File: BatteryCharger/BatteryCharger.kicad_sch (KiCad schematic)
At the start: 6 parts, among them Q1 SiR638DP, Q2 SiR638DP, Q3 SiR500DP, Q4 BSC059N04LS6, Q5 SQJ868EP, U1 BQ24735

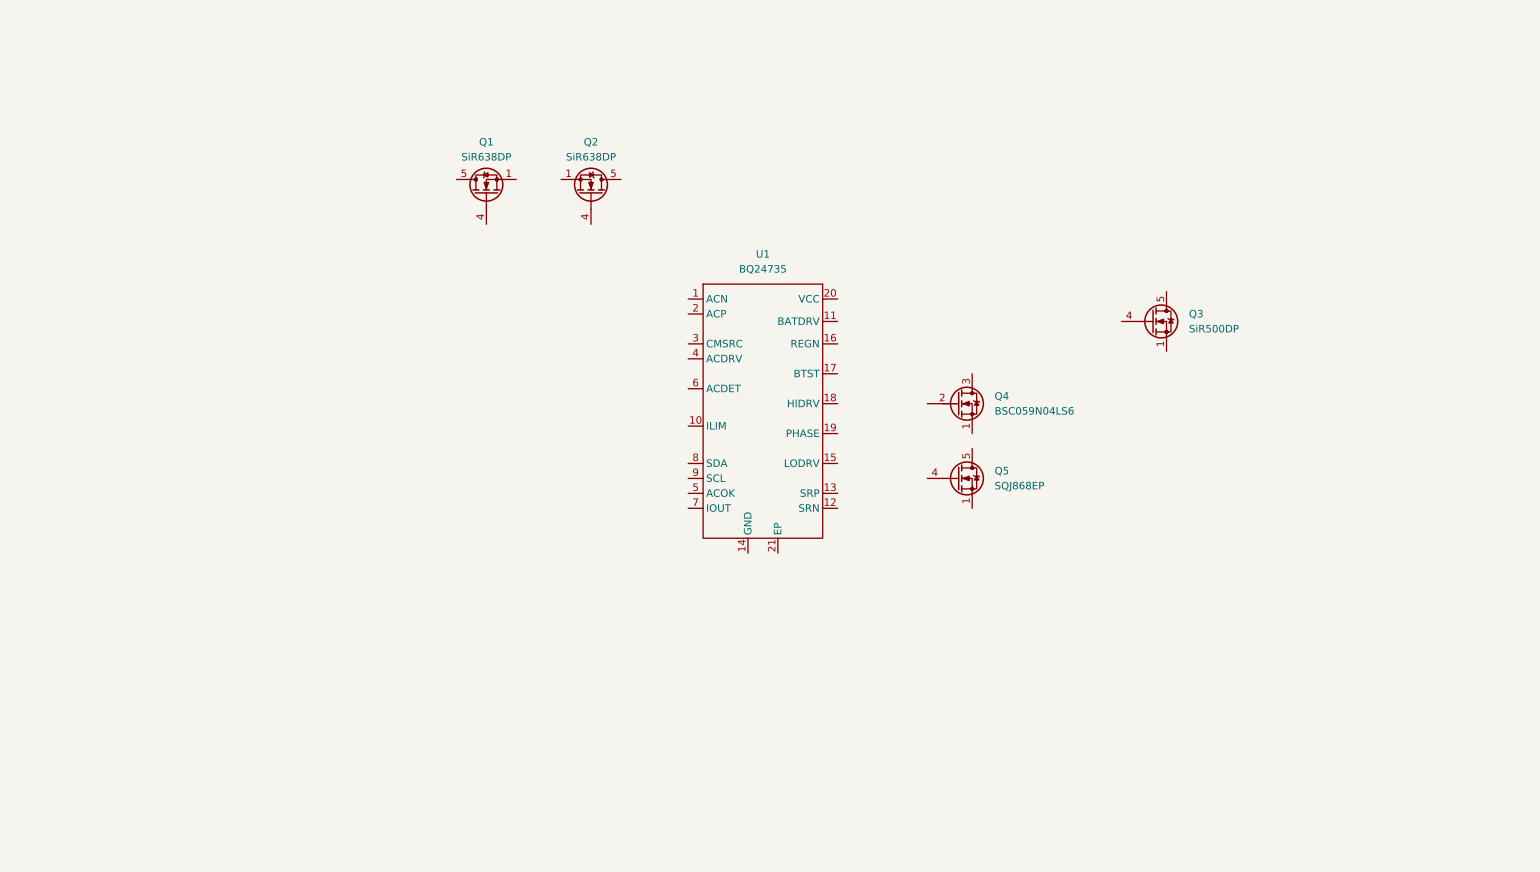
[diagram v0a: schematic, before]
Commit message: BatteryCharger schematic initially done
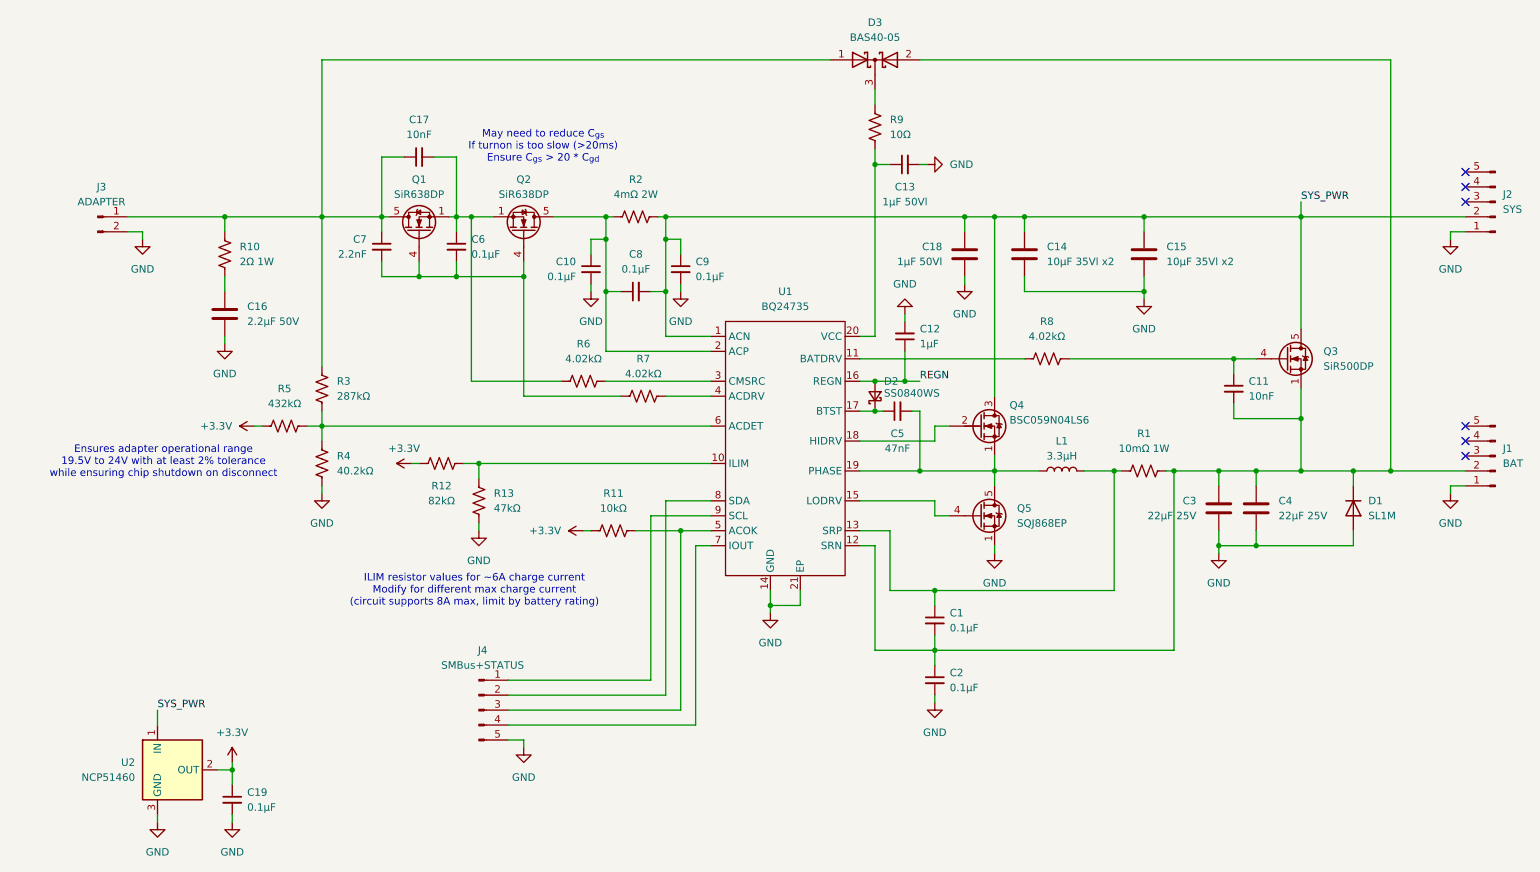
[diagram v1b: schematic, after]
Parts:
- added C1, C10, C19, C2, C6, C8, C9: 0.1µF, Capacitor_SMD:C_0603_1608Metric, symbol Device:C_Small
- added C11, C17: 10nF, Capacitor_SMD:C_0603_1608Metric, symbol Device:C_Small
- added C12: 1µF, Capacitor_SMD:C_0603_1608Metric, symbol Device:C_Small
- added C13: 1µF 50Vl, Capacitor_SMD:C_0805_2012Metric, symbol Device:C_Small
- added C14, C15: 10µF 35Vl x2, Capacitor_SMD:C_1210_3225Metric, symbol Device:C
- added C16: 2.2µF 50V, Capacitor_SMD:C_0805_2012Metric, symbol Device:C
- added C18: 1µF 50Vl, Capacitor_SMD:C_0805_2012Metric, symbol Device:C
- added C3, C4: 22µF 25V, Capacitor_SMD:C_1210_3225Metric, symbol Device:C
- added C5: 47nF, Capacitor_SMD:C_0603_1608Metric, symbol Device:C_Small
- added C7: 2.2nF, Capacitor_SMD:C_0603_1608Metric, symbol Device:C_Small
- added D1: SL1M, Diode_SMD:D_SOD-123F, symbol Device:D
- added D2: SS0840WS, Diode_SMD:D_SOD-323_HandSoldering, symbol Device:D_Schottky_Small
- added D3: BAS40-05, Package_TO_SOT_SMD:SOT-23, symbol Device:D_Schottky_Dual_CommonCathode_AAK
- added J1: BAT, BW_Connectors:TE_2042274_Solder, symbol Connector:Conn_01x05_Pin
- added J2: SYS, BW_Connectors:TE_2042274_Solder, symbol Connector:Conn_01x05_Pin
- added J3: ADAPTER, BW_Connectors:Molex_Mini-Fit_Max_2P_V_215915-1002, symbol Connector:Conn_01x02_Pin
- added J4: SMBus+STATUS, BW_Connectors:Amphenol_MINITEK_WTB_1.25_5P, symbol Connector:Conn_01x05_Pin
- added L1: 3.3µH, BW_PassiveMechanical:L_Eaton_EXL1V0703, symbol Device:L
- added R1: 10mΩ 1W, Resistor_SMD:R_1206_3216Metric, symbol Device:R_US
- added R10: 2Ω 1W, BW_PassiveMechanical:R_0508_1220Metric, symbol Device:R_US
- added R11: 10kΩ, Resistor_SMD:R_0603_1608Metric, symbol Device:R_US
- added R12: 82kΩ, Resistor_SMD:R_0603_1608Metric, symbol Device:R_US
- added R13: 47kΩ, Resistor_SMD:R_0603_1608Metric, symbol Device:R_US
- added R2: 4mΩ 2W, Resistor_SMD:R_0612_1632Metric, symbol Device:R_US
- added R3: 287kΩ, Resistor_SMD:R_0603_1608Metric, symbol Device:R_US
- added R4: 40.2kΩ, Resistor_SMD:R_0603_1608Metric, symbol Device:R_US
- added R5: 432kΩ, Resistor_SMD:R_0603_1608Metric, symbol Device:R_US
- added R6, R7, R8: 4.02kΩ, Resistor_SMD:R_0603_1608Metric, symbol Device:R_US
- added R9: 10Ω, Resistor_SMD:R_0603_1608Metric, symbol Device:R_US
- added U2: NCP51460, Package_TO_SOT_SMD:SOT-23, symbol BW_Active:NCP51460
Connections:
- net at Q3.1 (S), Q3.2 (S), Q3.3 (S): now also U1.12 (SRN), C1.2, C11.2, C2.1, C3.1, C4.1, D1.1 (K), D3.2 (A), J1.2 (Pin_2), R1.2
- net at Q3.4 (G): now also C11.1, R8.2
- net SYS_PWR: now reaches Q3.5 (D)
- net SYS_PWR: now also Q4.3 (D), U1.1 (ACN), C14.1, C15.1, C18.1, C8.2, C9.1, J2.2 (Pin_2), R2.2, U2.1 (IN)
- net at U1.10 (ILIM): now also R12.2, R13.2
- net at U1.11 (BATDRV): now also R8.1
- net at U1.13 (SRP): now also C1.1, L1.2, R1.1
- net GND: now reaches U1.14 (GND)
- net GND: now also Q5.1 (S), Q5.2 (S), Q5.3 (S), U1.21 (EP), C10.2, C12.2, C13.2, C14.2, C15.2, C16.2, C18.2, C19.2, C2.2, C3.2, C4.2, C9.2, D1.2 (A), J1.1 (Pin_1), J2.1 (Pin_1), J3.2 (Pin_2), J4.5 (Pin_5), R13.1, R4.2, U2.3 (GND)
- net at U1.15 (LODRV): now also Q5.4 (G)
- net REGN: now reaches U1.16 (REGN)
- net REGN: now also C12.1, D2.2 (A)
- net at U1.17 (BTST): now also C5.1, D2.1 (K)
- net at U1.18 (HIDRV): now also Q4.2 (G)
- net at U1.19 (PHASE): now also Q4.1 (S), Q5.5 (D), C5.2, L1.1
- net at U1.2 (ACP): now also Q2.5 (D), C10.1, C8.1, R2.1
- net at U1.20 (VCC): now also C13.1, R9.2
- net at U1.3 (CMSRC): now also R6.2
- net at U1.4 (ACDRV): now also R7.2
- net at U1.5 (ACOK): now also J4.3 (Pin_3), R11.2
- net at U1.6 (ACDET): now also R3.2, R4.1, R5.2
- net at U1.7 (IOUT): now also J4.4 (Pin_4)
- net at U1.8 (SDA): now also J4.2 (Pin_2)
- net at U1.9 (SCL): now also J4.1 (Pin_1)
- net at Q2.1 (S), Q2.2 (S), Q2.3 (S): now also Q1.1 (S), Q1.2 (S), Q1.3 (S), C17.2, C6.1, R6.1
- net at Q2.4 (G): now also Q1.4 (G), C6.2, C7.2, R7.1
- net at Q1.5 (D): now also C17.1, C7.1, D3.1 (A), J3.1 (Pin_1), R10.1, R3.1
- new net: C16.1, R10.2
- new net: D3.3 (K), R9.1
- new net +3.3V: C19.1, R11.1, R12.1, R5.1, U2.2 (OUT)
- no-connect marks 0 -> 6
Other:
- note added: "Ensures adapter operational range 19.5V to 24V with at least 2% tolerance while ensuring chip shutdown on disconnect"
- note added: "ILIM resistor values for ~6A charge current Modify for different max charge current (circuit supports 8A max, limit by battery rating)"
- note added: "May need to reduce C_{gs} If turnon is too slow (>20ms) Ensure C_{gs} > 20 * C_{gd}"
- moved on the sheet: Q1, Q2, Q3, Q4, Q5, U1

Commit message: BatteryCharger pcb progress
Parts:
- removed C4: 22µF 25V, Capacitor_SMD:C_1210_3225Metric, symbol Device:C
- C15: renamed from C3; value 22µF 25V -> 22µF 25V x2
- R11: renamed from R1; value 10mΩ 1W -> 10mΩ 1.5W; footprint Resistor_SMD:R_1206_3216Metric -> Resistor_SMD:R_0612_1632Metric
- renumbered C17 to C1, C8 to C10, C16 to C11, C11 to C13, C5 to C14, C1 to C16, C2 to C17, C19 to C18, C13 to C2, C7 to C3, C6 to C4, C18 to C5, C14 to C6, C15 to C7, C10 to C8, D3 to D1, D1 to D3, J2 to J1, J3 to J2, J1 to J3, R9 to R1, R12 to R10, R13 to R12, R11 to R13, R10 to R3, R8 to R4, R6 to R5, R3 to R6, R5 to R8, R4 to R9
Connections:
- net GND: now also J2.1 (Pin_1); no longer J2.2 (Pin_2)
- net at C1.1, C3.1, D1.1 (A)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: now also J2.2 (Pin_2); no longer J2.1 (Pin_1)
- net at C13.2, C15.1, C16.2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: now also J3.3 (Pin_3), J3.4 (Pin_4), J3.5 (Pin_5)
- no-connect marks 6 -> 3
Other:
- moved on the sheet: C15

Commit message: BatteryCharger board initially done
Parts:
- added J5, J6: GND_BRIDGE, BW_PassiveMechanical:HolePad_2.5mm_3.5mm, symbol Connector:Conn_01x01_Pin
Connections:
- net GND: now also J5.1 (Pin_1), J6.1 (Pin_1)
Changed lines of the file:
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@@
 	)
 	(junction
+		(at 261.62 110.49)
+		(diameter 0)
+		(color 0 0 0 0)
+	)
+	(junction
 		(at 118.11 68.58)
 		(diameter 0)
@@
 	)
 	(junction
+		(at 261.62 67.31)
+		(diameter 0)
+		(color 0 0 0 0)
+	)
+	(junction
 		(at 204.47 107.95)
 		(diameter 0)
@@
 	(wire
 		(pts
+			(xy 256.54 116.84) (xy 256.54 110.49)
+		)
+		(stroke
+			(width 0)
+			(type default)
+		)
+	)
+	(wire
+		(pts
 			(xy 264.16 100.33) (xy 261.62 100.33)
 		)
@@
 	(wire
 		(pts
+			(xy 256.54 73.66) (xy 256.54 67.31)
+		)
+		(stroke
+			(width 0)
+			(type default)
+		)
+	)
+	(wire
+		(pts
 			(xy 161.29 92.71) (xy 163.83 92.71)
 		)
@@
 	(wire
 		(pts
+			(xy 256.54 67.31) (xy 261.62 67.31)
+		)
+		(stroke
+			(width 0)
+			(type default)
+		)
+	)
+	(wire
+		(pts
 			(xy 166.37 118.11) (xy 166.37 128.27)
 		)
@@
 	(wire
 		(pts
+			(xy 256.54 110.49) (xy 261.62 110.49)
+		)
+		(stroke
+			(width 0)
+			(type default)
+		)
+	)
+	(wire
+		(pts
 			(xy 163.83 55.88) (xy 163.83 85.09)
 		)
@@
 	)
 	(symbol
+		(lib_id "Connector:Conn_01x01_Pin")
+		(at 256.54 78.74 90)
+		(unit 1)
+		(exclude_from_sim no)
+		(in_bom yes)
+		(on_board yes)
+		(dnp no)
+		(fields_autoplaced yes)
+		(property "Reference" "J6"
+			(at 257.81 76.8349 90)
+			(effects
+				(font
+					(size 1.27 1.27)
+				)
+				(justify right)
+			)
+		)
+		(property "Value" "GND_BRIDGE"
+			(at 257.81 79.3749 90)
+			(effects
+				(font
+					(size 1.27 1.27)
+				)
+				(justify right)
+			)
+		)
+		(property "Footprint" "BW_PassiveMechanical:HolePad_2.5mm_3.5mm"
+			(at 256.54 78.74 0)
+			(effects
+				(font
+					(size 1.27 1.27)
+				)
+				(hide yes)
+			)
+		)
+		(property "Datasheet" "~"
+			(at 256.54 78.74 0)
+			(effects
+				(font
+					(size 1.27 1.27)
+				)
+				(hide yes)
+			)
+		)
+		(property "Description" "Generic connector, single row, 01x01, script generated"
+			(at 256.54 78.74 0)
+			(effects
+				(font
+					(size 1.27 1.27)
+				)
+				(hide yes)
+			)
+		)
+		(pin "1"
+		)
+		(instances
+			(project "BatteryCharger"
+				(path "/2812e6ed-be62-4845-b36d-492b76fd9757"
+					(reference "J6")
+					(unit 1)
+				)
+			)
+		)
+	)
+	(symbol
 		(lib_id "power:GND")
 		(at 261.62 68.58 0)
@@
 					(unit 1)
 				)
+			)
+		)
+	)
+	(symbol
+		(lib_id "Connector:Conn_01x01_Pin")
+		(at 256.54 121.92 90)
+		(unit 1)
+		(exclude_from_sim no)
+		(in_bom yes)
+		(on_board yes)
+		(dnp no)
+		(fields_autoplaced yes)
+		(property "Reference" "J5"
+			(at 257.81 120.0149 90)
+			(effects
+				(font
+					(size 1.27 1.27)
+				)
+				(justify right)
+			)
+		)
+		(property "Value" "GND_BRIDGE"
+			(at 257.81 122.5549 90)
+			(effects
+				(font
+					(size 1.27 1.27)
+				)
+				(justify right)
+			)
+		)
+		(property "Footprint" "BW_PassiveMechanical:HolePad_2.5mm_3.5mm"
+			(at 256.54 121.92 0)
+			(effects
+				(font
+					(size 1.27 1.27)
+				)
+				(hide yes)
+			)
+		)
+		(property "Datasheet" "~"
+			(at 256.54 121.92 0)
+			(effects
+				(font
+					(size 1.27 1.27)
+				)
+				(hide yes)
+			)
+		)
+		(property "Description" "Generic connector, single row, 01x01, script generated"
+			(at 256.54 121.92 0)
+			(effects
+				(font
+					(size 1.27 1.27)
+				)
+				(hide yes)
+			)
+		)
+		(pin "1"
+		)
+		(instances
+			(project ""
+				(path "/2812e6ed-be62-4845-b36d-492b76fd9757"
+					(reference "J5")
+					(unit 1)
+				)

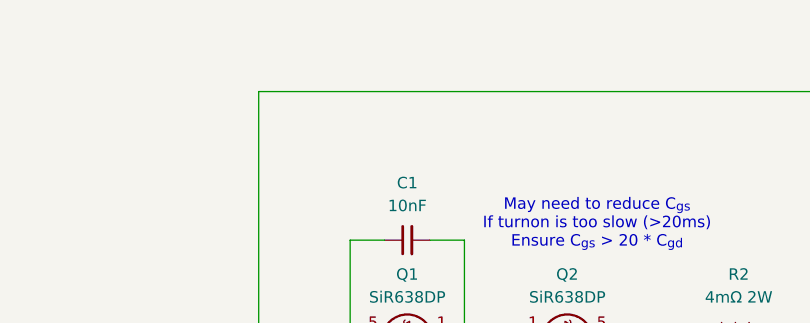
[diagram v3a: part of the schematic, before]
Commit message: BatteryMonitor and BatteryCharger inventory order
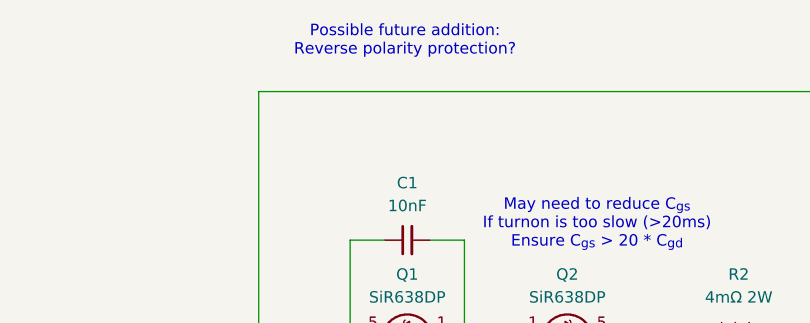
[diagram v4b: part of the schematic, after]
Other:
- note added: "Possible future addition: Reverse polarity protection?"
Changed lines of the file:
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@@
+		)
+	)
+	(text "Possible future addition:\nReverse polarity protection?"
+		(exclude_from_sim no)
+		(at 86.106 32.512 0)
+		(effects
+			(font
+				(size 1.27 1.27)
+			)
 		)
 	)

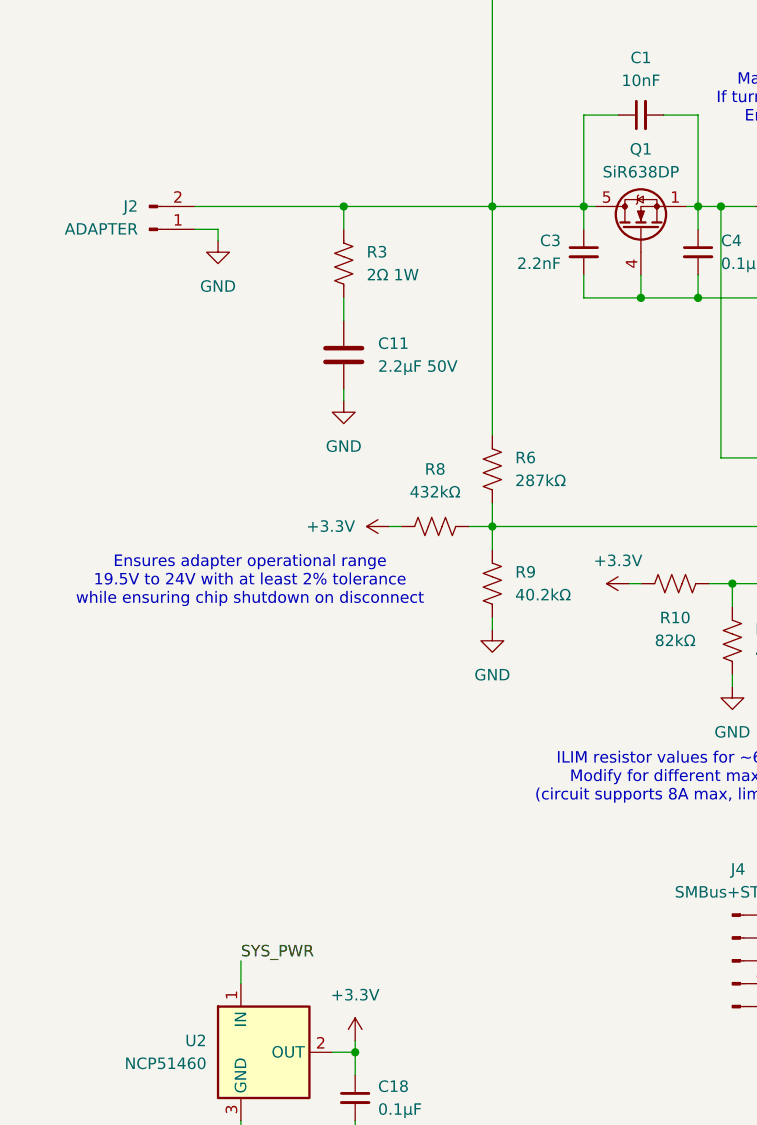
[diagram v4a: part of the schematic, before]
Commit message: BatteryCharger testing + small fix
U2 voltage source was incorrect
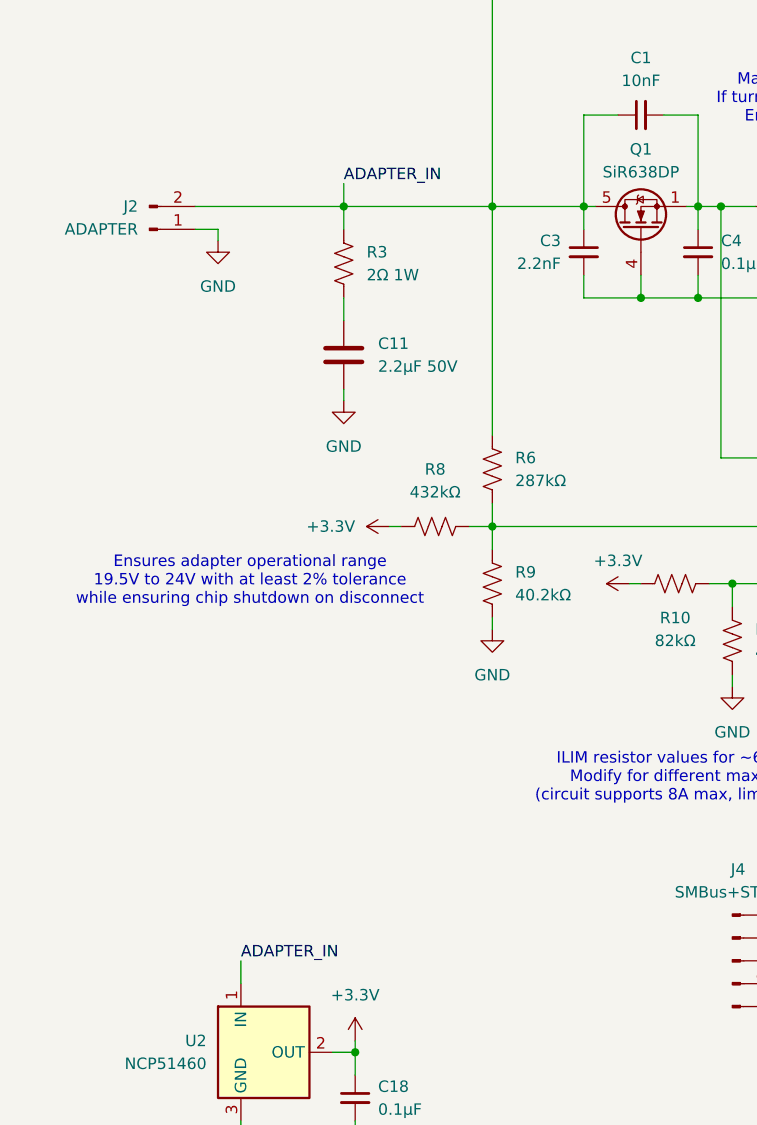
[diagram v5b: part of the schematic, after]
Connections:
- net SYS_PWR: no longer U2.1 (IN)
- net ADAPTER_IN: now reaches C1.1, C3.1, D1.1 (A), J2.2 (Pin_2), Q1.5 (D), R3.1, R6.1
- net ADAPTER_IN: now also U2.1 (IN)
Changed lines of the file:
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@@
+	(wire
+		(pts
+			(xy 53.34 62.23) (xy 53.34 64.77)
+		)
+		(stroke
+			(width 0)
+			(type default)
+		)
+	)
 	(wire
 		(pts
@@
 	(label "REGN"
 		(at 171.45 92.71 0)
-		(fields_autoplaced yes)
 		(effects
 			(font
@@
 		)
 	)
-	(label "SYS_PWR"
+	(label "ADAPTER_IN"
 		(at 41.91 148.59 0)
-		(fields_autoplaced yes)
+		(effects
+			(font
+				(size 1.27 1.27)
+			)
+			(justify left bottom)
+		)
+	)
+	(label "ADAPTER_IN"
+		(at 53.34 62.23 0)
 		(effects
 			(font
@@
 	(label "SYS_PWR"
 		(at 236.22 62.23 0)
-		(fields_autoplaced yes)
 		(effects
 			(font
